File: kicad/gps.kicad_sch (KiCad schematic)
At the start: 66 parts, among them J1 Bus_PCI_Express_x1, J2 USB_C_Receptacle_USB2.0_16P, J3 Conn_01x02, J4 USB_C_Receptacle_USB2.0_16P, Q1 IRLML6344, U2 W25Q128JVP, U3 MCP25625T-E/ML, U4 RP2040, U5 NEO-M9N, X1 ABM8-272-T3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

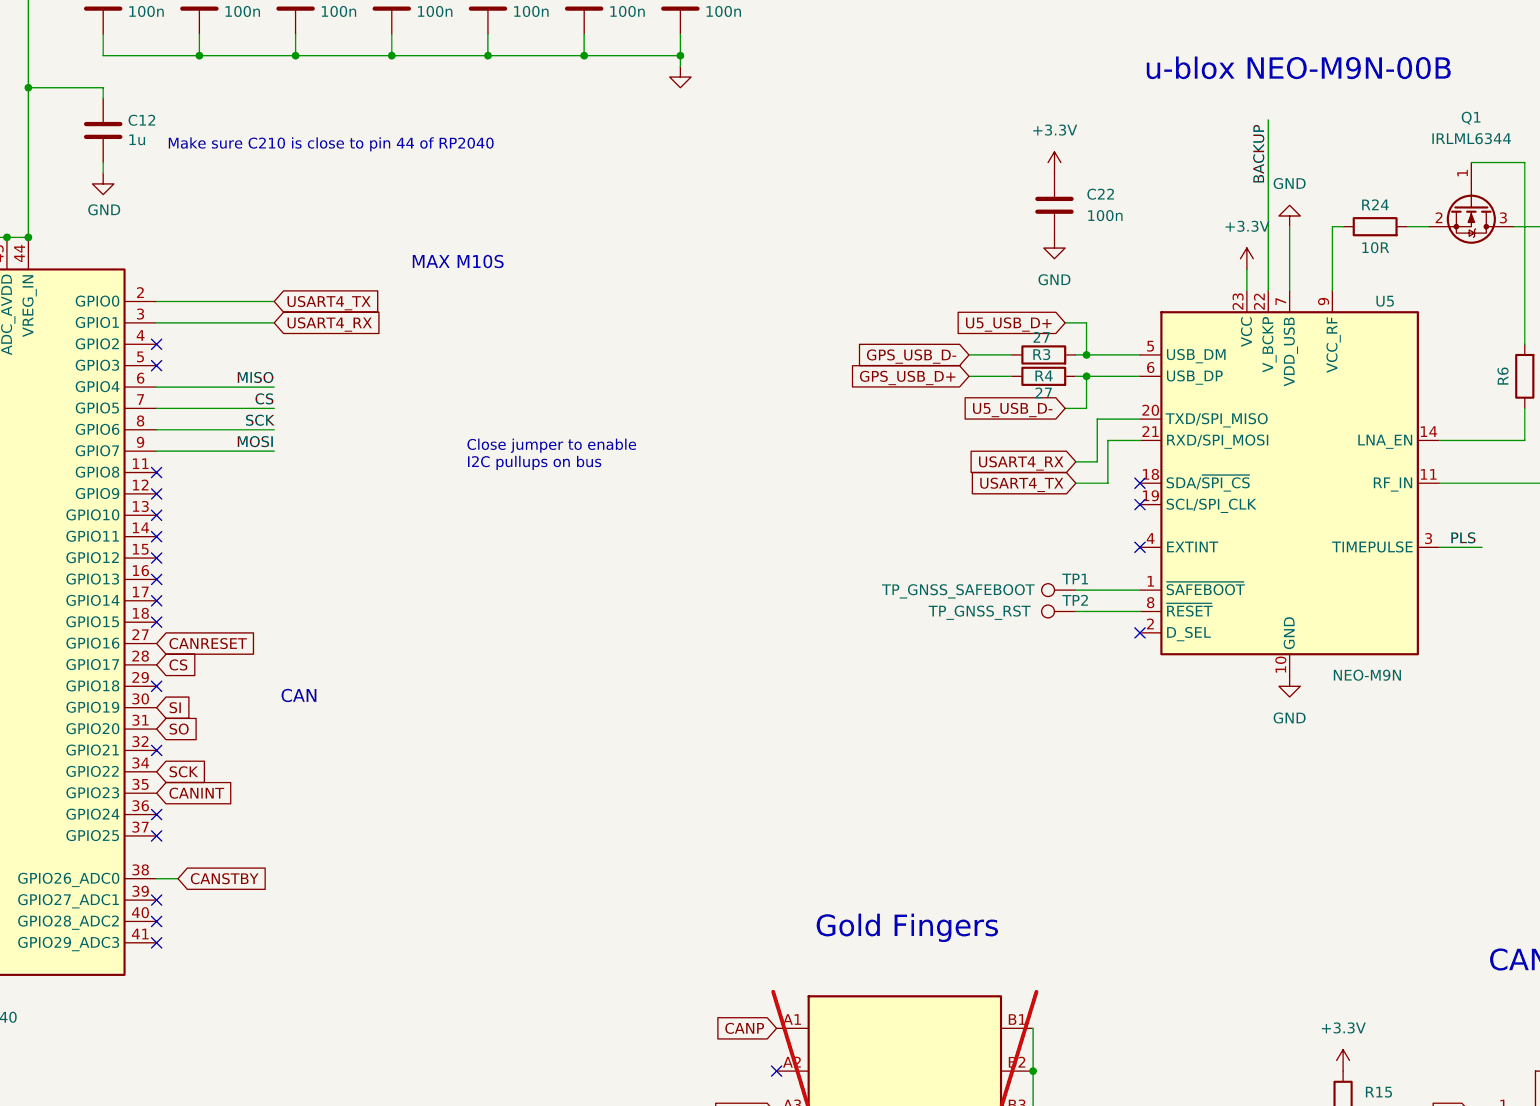
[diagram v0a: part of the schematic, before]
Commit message: Finish GPS routing and LNA control
- Added LNA_EN switch circuit with IRLML6344
- Finalized VCC_RF routing and return path
- Cleaned up UART1 connection on GPIO28/29
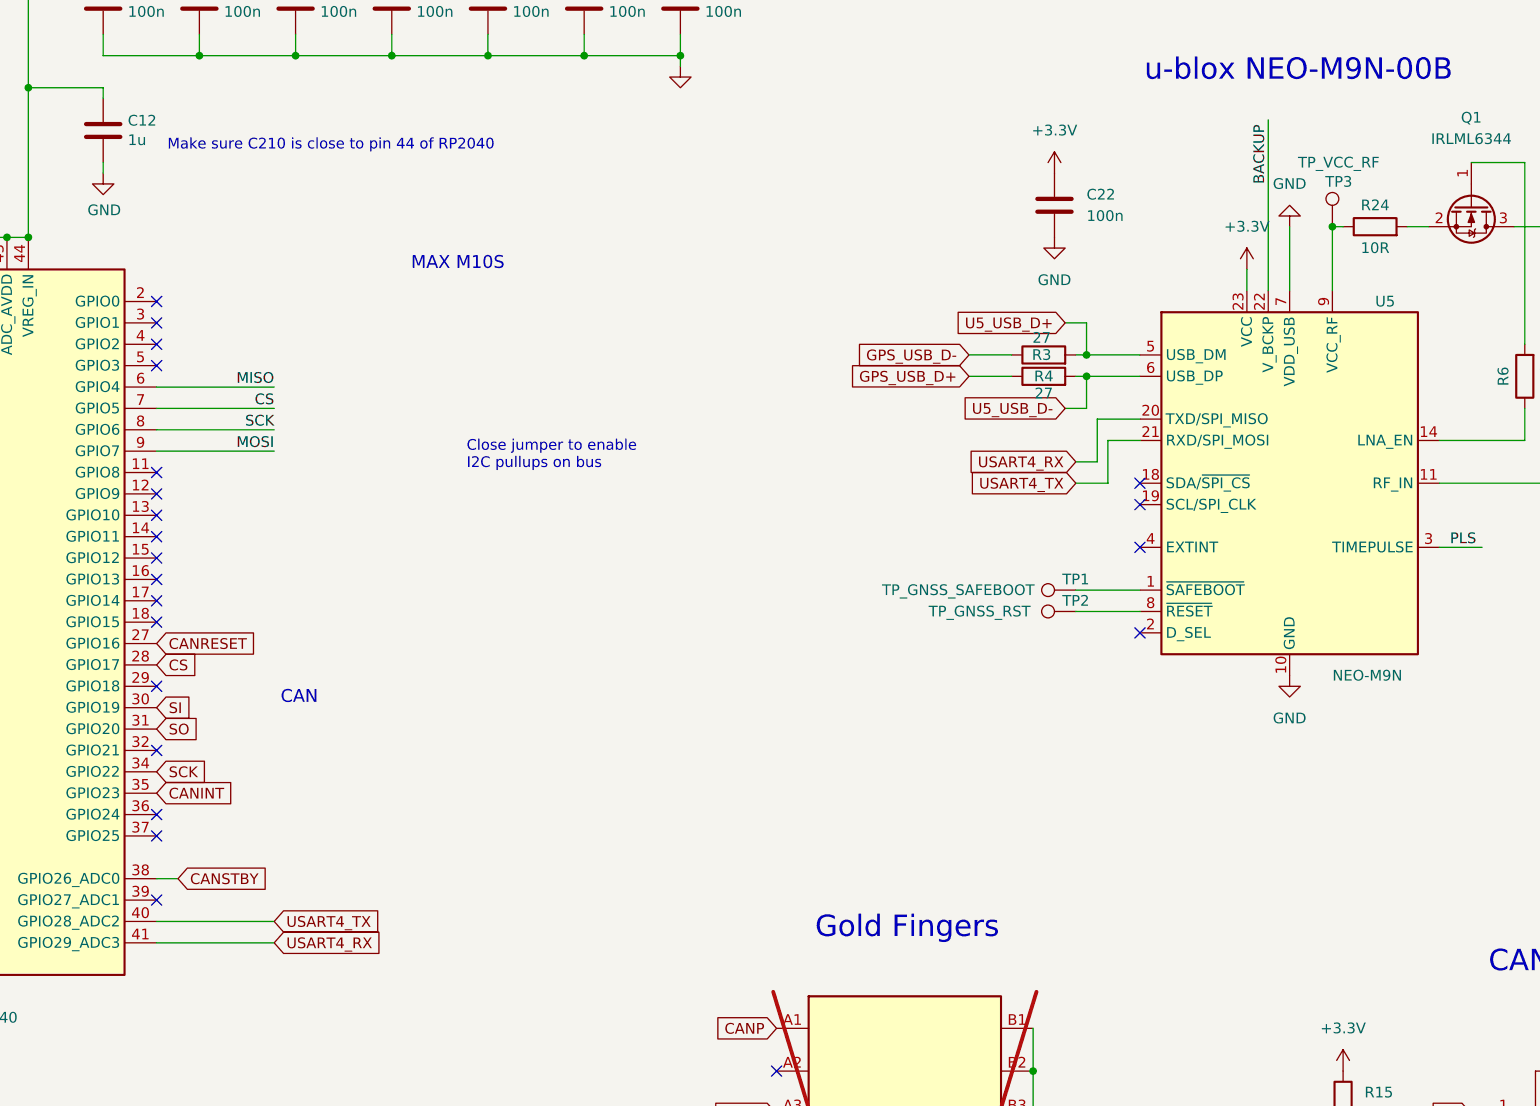
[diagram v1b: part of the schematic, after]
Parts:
- added TP3: TP_VCC_RF, TestPoint:TestPoint_Pad_D1.0mm, symbol Connector:TestPoint
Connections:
- net USART4_RX: now also U4.41 (GPIO29_ADC3); no longer U4.3 (GPIO1)
- net USART4_TX: now also U4.40 (GPIO28_ADC2); no longer U4.2 (GPIO0)
- net at R24.1, U5.9 (VCC_RF): now also TP3.1
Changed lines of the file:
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@@
 	)
 	(junction
+		(at 270.51 66.04)
+		(diameter 0)
+		(color 0 0 0 0)
+	)
+	(junction
 		(at 109.22 180.34)
 		(diameter 0)
@@
 	)
 	(no_connect
-		(at 130.81 151.13)
-	)
-	(no_connect
 		(at 287.02 191.77)
 	)
@@
 	)
 	(no_connect
+		(at 130.81 74.93)
+	)
+	(no_connect
 		(at 175.26 237.49)
 	)
@@
 	)
 	(no_connect
-		(at 130.81 148.59)
-	)
-	(no_connect
 		(at 234.95 242.57)
 	)
@@
 	)
 	(no_connect
+		(at 130.81 77.47)
+	)
+	(no_connect
 		(at 130.81 120.65)
 	)
@@
 	(wire
 		(pts
-			(xy 130.81 74.93) (xy 144.78 74.93)
-		)
-		(stroke
-			(width 0)
-			(type default)
-		)
-	)
-	(wire
-		(pts
 			(xy 107.95 67.31) (xy 110.49 67.31)
 		)
@@
 	(wire
 		(pts
+			(xy 130.81 151.13) (xy 144.78 151.13)
+		)
+		(stroke
+			(width 0)
+			(type default)
+		)
+	)
+	(wire
+		(pts
 			(xy 99.06 199.39) (xy 82.55 199.39)
 		)
@@
 	(wire
 		(pts
-			(xy 130.81 77.47) (xy 144.78 77.47)
-		)
-		(stroke
-			(width 0)
-			(type default)
-		)
-	)
-	(wire
-		(pts
 			(xy 384.81 69.85) (xy 384.81 72.39)
 		)
@@
 	(wire
 		(pts
+			(xy 130.81 148.59) (xy 144.78 148.59)
+		)
+		(stroke
+			(width 0)
+			(type default)
+		)
+	)
+	(wire
+		(pts
 			(xy 204.47 227.33) (xy 204.47 222.25)
 		)
@@
 		)
 	)
+	(global_label "USART4_TX"
+		(shape input)
+		(at 144.78 148.59 0)
+		(fields_autoplaced yes)
+		(effects
+			(font
+				(size 1.27 1.27)
+			)
+			(justify left)
+		)
+		(property "Intersheetrefs" "${INTERSHEET_REFS}"
+			(at 157.9856 148.59 0)
+			(effects
+				(font
+					(size 1.27 1.27)
+				)
+				(justify left)
+				(hide yes)
+			)
+		)
+	)
 	(global_label "CANSTBY"
 		(shape input)
@@
 		)
 	)
+	(global_label "USART4_RX"
+		(shape input)
+		(at 144.78 151.13 0)
+		(fields_autoplaced yes)
+		(effects
+			(font
+				(size 1.27 1.27)
+			)
+			(justify left)
+		)
+		(property "Intersheetrefs" "${INTERSHEET_REFS}"
+			(at 158.288 151.13 0)
+			(effects
+				(font
+					(size 1.27 1.27)
+				)
+				(justify left)
+				(hide yes)
+			)
+		)
+	)
 	(global_label "CANP"
 		(shape input)
@@
 		)
 	)
-	(global_label "USART4_TX"
-		(shape input)
-		(at 144.78 74.93 0)
-		(fields_autoplaced yes)
-		(effects
-			(font
-				(size 1.27 1.27)
-			)
-			(justify left)
-		)
-		(property "Intersheetrefs" "${INTERSHEET_REFS}"
-			(at 157.9856 74.93 0)
-			(effects
-				(font
-					(size 1.27 1.27)
-				)
-				(justify left)
-				(hide yes)
-			)
-		)
-	)
 	(global_label "CANRESET"
 		(shape input)
@@
 		)
 	)
-	(global_label "USART4_RX"
-		(shape input)
-		(at 144.78 77.47 0)
-		(fields_autoplaced yes)
-		(effects
-			(font
-				(size 1.27 1.27)
-			)
-			(justify left)
-		)
-		(property "Intersheetrefs" "${INTERSHEET_REFS}"
-			(at 158.288 77.47 0)
-			(effects
-				(font
-					(size 1.27 1.27)
-				)
-				(justify left)
-				(hide yes)
-			)
-		)
-	)
 	(symbol
 		(lib_id "SparkFun u-blox GNSS MAX-M10S-eagle-import:3.3V")
@@
 					(unit 1)
 				)
+			)
+		)
+	)
+	(symbol
+		(lib_id "Connector:TestPoint")
+		(at 270.51 66.04 0)
+		(unit 1)
+		(exclude_from_sim no)
+		(in_bom yes)
+		(on_board yes)
+		(dnp no)
+		(property "Reference" "TP3"
+			(at 271.272 60.706 0)
+			(effects
+				(font
+					(size 1.27 1.27)
+				)
+			)
+		)
+		(property "Value" "TP_VCC_RF"
+			(at 271.272 58.42 0)
+			(effects
+				(font
+					(size 1.27 1.27)
+				)
+			)
+		)
+		(property "Footprint" "TestPoint:TestPoint_Pad_D1.0mm"
+			(at 275.59 66.04 0)
+			(effects
+				(font
+					(size 1.27 1.27)
+				)
+				(hide yes)
+			)
+		)
+		(property "Datasheet" "~"
+			(at 275.59 66.04 0)
+			(effects
+				(font
+					(size 1.27 1.27)
+				)
+				(hide yes)
+			)
+		)
+		(property "Description" ""
+			(at 270.51 66.04 0)
+			(effects
+				(font
+					(size 1.27 1.27)
+				)
+				(hide yes)
+			)
+		)
+		(pin "1"
+		)
+		(instances
+			(project "gps"
+				(path "/e1ff46b9-0cf9-4507-8034-1e95fc3013fc"
+					(reference "TP3")
+					(unit 1)
+				)

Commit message: Update all component properites
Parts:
- removed C23: 100n 10% 16V X7R, Capacitor_SMD:C_0402_1005Metric, symbol Device:C
- added C1: 100n, Capacitor_SMD:C_0402_1005Metric, symbol Device:C
- C22: JLC Link (none) -> https://jlcpcb.com/partdetail/291005-CL05B104KB54PNC/C307331; LCSC Part C15195 -> (none); LCSC Part # C15195 -> C307331; basic? (none) -> yes; info (none) -> 100nF Cap; price (none) -> C$0.0077
- C7: value 1uF -> 1u; JLC Link (none) -> https://jlcpcb.com/partdetail/53938-CL05A105KA5NQNC/C52923; LCSC Part # (none) -> C52923; price (none) -> C$0.0041
- D2: Basic? (none) -> Yes; Current Draw (none) -> 500 mA average forward current (IF(av)); up to 5 A peak for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; Height (none) -> 1.1 mm (typical for SOD-323); Info (none) -> Schottky Barrier Diode, 40 V, 500 mA (avg fwd current), low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; JLC Link (none) -> https://jlcpcb.com/partdetail/Nexperia-PMEG4005EJ115/C426868; LCSC Part # (none) -> C426868; Manufacturer Name (none) -> Nexperia; Manufacturer Part Number (none) -> PMEGA4005EJ,115; Mouser Part Number (none) -> 771-PMEG4005EJ115; Mouser Price/Stock (none) -> ~C$0.11 / In Stock; Notes (none) -> Forward voltage: ~0.36 V at 100 mA; reverse current: ~2 μA;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; Price (none) -> ~C$0.026 (in bulk)
- L1: footprint Inductor_SMD:L_0603_1608Metric -> Resistor_SMD:R_0402_1005Metric; Basic? (none) -> Yes; Current Draw (none) -> Rated current: 350 mA; Height (none) -> 0.5 mm; Info (none) -> 27 nH ±5%, 0402 SMD inductor, High-Frequency Series (LQG15H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; JLC Link (none) -> https://jlcpcb.com/partdetail/MurataElectronics-LQG15HS27NJ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; LCSC Part # (none) -> C12669; Manufacturer Name (none) -> Murata Electronics; Manufacturer Part Number (none) -> LQG15HS27NJ02D; Mouser Part Number (none) -> 81-LQG15HS27NJ02D; Mouser Price/Stock (none) -> ~C$0.16 / In Stock; Notes (none) -> DCR: 0.46 Ω; Self-resonant frequency: ~1.9 GHz; High Q, des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; Price (none) -> ~C$0.006 per unit (bulk pricing)
- Q1: Basic? (none) -> No; Current Draw (none) -> Continuous Drain Current: 5 A (at 25 °C); Height (none) -> 1.1 mm; Info (none) -> N-Channel Power MOSFET, 30 V, 5 A, SOT-23 package; JLC Link (none) -> https://jlcpcb.com/partdetail/GuangdongHottech-IRLML6344/C5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; LCSC Part # (none) -> C5364313; Manufacturer Name (none) -> Guangdong Hottech; Manufacturer Part Number (none) -> IRLML6344; Mouser Part Number (none) -> N/A; Mouser Price/Stock (none) -> N/A; Notes (none) -> R<sub>DS(on)</sub>: 29 mΩ @ V<sub>GS</sub> = 4.5 V; Gate th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; Price (none) -> C$0.064 (approximate)
- R20, R22: JLC Link (none) -> https://jlcpcb.com/partdetail/12256-0402WGF1001TCE/C11702; LCSC Part # (none) -> C11702; info (none) -> 1k ohm; price C$0.0007 -> C$0.0007
- R24: Basic? (none) -> Yes; Current Draw (none) -> N/A (passive component); Height (none) -> Approximately 0.4 mm; Info (none) -> Thick Film Chip Resistor, 10 Ω, 0402 package, ±1% tolerance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; JLC Link (none) -> https://jlcpcb.com/partdetail/25820-0402WGF100JTCE/C25077; LCSC Part # (none) -> C25077; Manufacturer Name (none) -> UNI-ROYAL (Uniroyal Elec); Manufacturer Part Number (none) -> 0402WGF100JTCE; Mouser Part Number (none) -> Not listed; Mouser Price/Stock (none) -> Not listed; Notes (none) -> Suitable for general-purpose surface-mount applications; Ro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; Price (none) -> Approximately C$0.0005 per unit (bulk pricing available)
- R5: Basic? (none) -> Yes; Current Draw (none) -> N/A (passive component); Height (none) -> Approximately 0.4 mm; Info (none) -> Thick Film Chip Resistor, 100 Ω, 0402 package, ±1% toleranc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; JLC Link (none) -> https://jlcpcb.com/partdetail/25821-0402WGF1000TCE/C25078; LCSC Part # (none) -> C25078; Manufacturer Name (none) -> UNI-ROYAL (Uniroyal Elec); Manufacturer Part Number (none) -> 0402WGF1000TCE; Mouser Part Number (none) -> Not listed; Mouser Price/Stock (none) -> Not listed; Notes (none) -> Suitable for general-purpose surface-mount applications; Ro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; Price (none) -> Approximately C$0.0005 per unit (bulk pricing available)
- R6: Basic? (none) -> Yes; Current Draw (none) -> N/A (passive component); Height (none) -> Approximately 0.35 mm; Info (none) -> Thick Film Chip Resistor, 10 kΩ, 0402 package, ±1% toleranc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; JLC Link (none) -> https://jlcpcb.com/partdetail/C25744; LCSC Part # (none) -> C25744; Manufacturer Name (none) -> UNI-ROYAL (Uniroyal Elec); Manufacturer Part Number (none) -> 0402WGF1002TCE; Mouser Part Number (none) -> Not listed; Mouser Price/Stock (none) -> Not listed; Notes (none) -> Suitable for general-purpose surface-mount applications; Ro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; Price (none) -> Approximately C$0.0005 per unit (bulk pricing available)
- U5: Basic? (none) -> No; Current Draw (none) -> ~29 mA (continuous tracking); Height (none) -> 2.4 mm; Info (none) -> GNSS Receiver Module (GPS, GLONASS, Galileo, BeiDou); JLC Link (none) -> https://jlcpcb.com/partdetail/ublox-NEO_M9N00B/C5119087; LCSC Part # (none) -> C5119087; Manufacturer Name (none) -> u-blox; Manufacturer Part Number (none) -> NEO-M9N-00B-00; Mouser Part Number (none) -> 377-NEO-M9N-00B-00; Mouser Price/Stock (none) -> C$19.60 / In Stock; Notes (none) -> Supports concurrent GNSS, UART/SPI/I2C, high update rate (u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; Price (none) -> C$15.1029
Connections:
- net +3.3V: now also C1.1; no longer C22.1
- net GND: now also C1.2
- net at L1.1, R5.1: now also C22.1
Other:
- moved on the sheet: J1

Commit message: Organize Schematic
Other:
- note added: "CAN Crystal"
- note added: "GPS Status LEDs"
- note added: "Power Status LEDs"
- note added: "RP2040 MCU"
- note removed: "Status LEDs"
- moved on the sheet: BAT1, C1, C10, C11, C12, C13, C14, C15, C16, C17, C18, C19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

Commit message: Fix DRC Violations
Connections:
- net CS: no longer U4.7 (GPIO5)
- net SCK: no longer U4.8 (GPIO6)
- net MISO: no longer names the net of U4.6 (GPIO4)
- net MOSI: no longer names the net of U4.9 (GPIO7)
- no-connect marks 44 -> 48
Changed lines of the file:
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@@
+	)
+	(no_connect
+		(at 123.19 88.9)
 	)
 	(no_connect
@@
 	)
 	(no_connect
+		(at 123.19 96.52)
+	)
+	(no_connect
 		(at 153.67 223.52)
 	)
 	(no_connect
+		(at 123.19 93.98)
+	)
+	(no_connect
 		(at 184.15 269.24)
 	)
@@
 	(no_connect
 		(at 123.19 109.22)
+	)
+	(no_connect
+		(at 123.19 91.44)
 	)
 	(no_connect
@@
 	(wire
 		(pts
-			(xy 123.19 91.44) (xy 137.16 91.44)
-		)
-		(stroke
-			(width 0)
-			(type default)
-		)
-	)
-	(wire
-		(pts
 			(xy 31.75 238.76) (xy 36.83 238.76)
 		)
@@
 	(wire
 		(pts
-			(xy 123.19 93.98) (xy 137.16 93.98)
-		)
-		(stroke
-			(width 0)
-			(type default)
-		)
-	)
-	(wire
-		(pts
 			(xy 280.67 30.48) (xy 274.32 30.48)
 		)
@@
 	(wire
 		(pts
-			(xy 123.19 88.9) (xy 137.16 88.9)
-		)
-		(stroke
-			(width 0)
-			(type default)
-		)
-	)
-	(wire
-		(pts
 			(xy 227.33 81.28) (xy 234.95 81.28)
 		)
@@
 		(pts
 			(xy 151.13 39.37) (xy 151.13 38.1)
-		)
-		(stroke
-			(width 0)
-			(type default)
-		)
-	)
-	(wire
-		(pts
-			(xy 123.19 96.52) (xy 137.16 96.52)
 		)
 		(stroke
@@
 		)
 	)
-	(label "CS"
-		(at 137.16 91.44 180)
-		(effects
-			(font
-				(size 1.27 1.27)
-			)
-			(justify right bottom)
-		)
-	)
 	(label "PLS"
 		(at 271.78 76.2 0)
@@
 		)
 	)
-	(label "MOSI"
-		(at 137.16 96.52 180)
-		(effects
-			(font
-				(size 1.27 1.27)
-			)
-			(justify right bottom)
-		)
-	)
 	(label "QSPI_SD2"
 		(at 58.42 106.68 0)
@@
 		)
 	)
-	(label "MISO"
-		(at 137.16 88.9 180)
-		(effects
-			(font
-				(size 1.27 1.27)
-			)
-			(justify right bottom)
-		)
-	)
 	(label "QSPI_SS"
 		(at 58.42 96.52 0)
@@
 		)
 	)
-	(label "SCK"
-		(at 137.16 93.98 180)
-		(effects
-			(font
-				(size 1.27 1.27)
-			)
-			(justify right bottom)
-		)
-	)

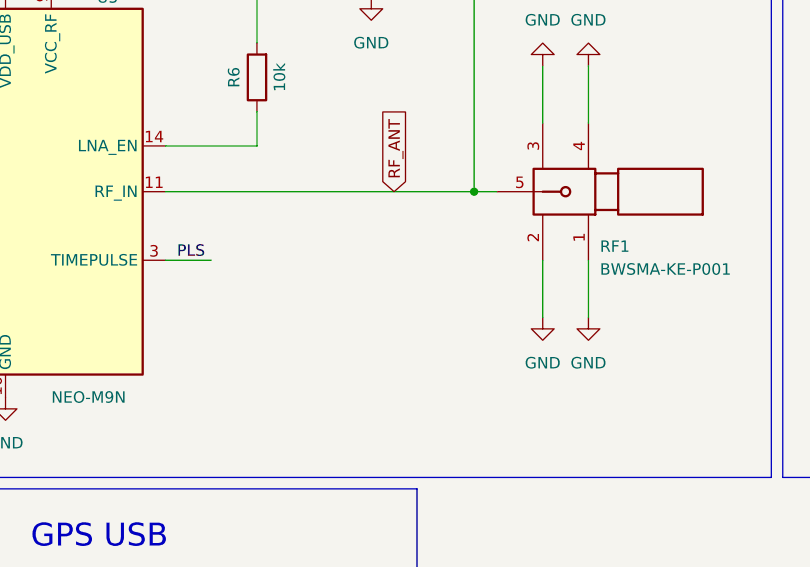
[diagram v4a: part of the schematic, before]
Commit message: Add TVS Diode
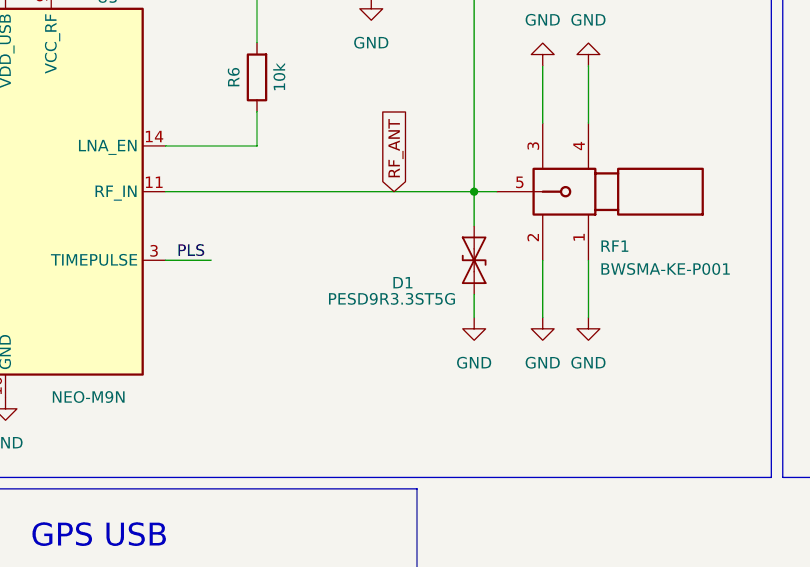
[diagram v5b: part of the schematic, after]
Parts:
- added D1: PESD9R3.3ST5G, Package_TO_SOT_SMD:SOD-923, symbol Diode:ESD9B3.3ST5G
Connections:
- net GND: now also D1.1 (A1)
- net RF_ANT: now also D1.2 (A2)
